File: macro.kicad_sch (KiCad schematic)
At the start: 27 parts, among them J1 USB_C_Receptacle_USB2.0, SW1 SW_Push, U1 ATmega32U4-A, Y1 16MHz

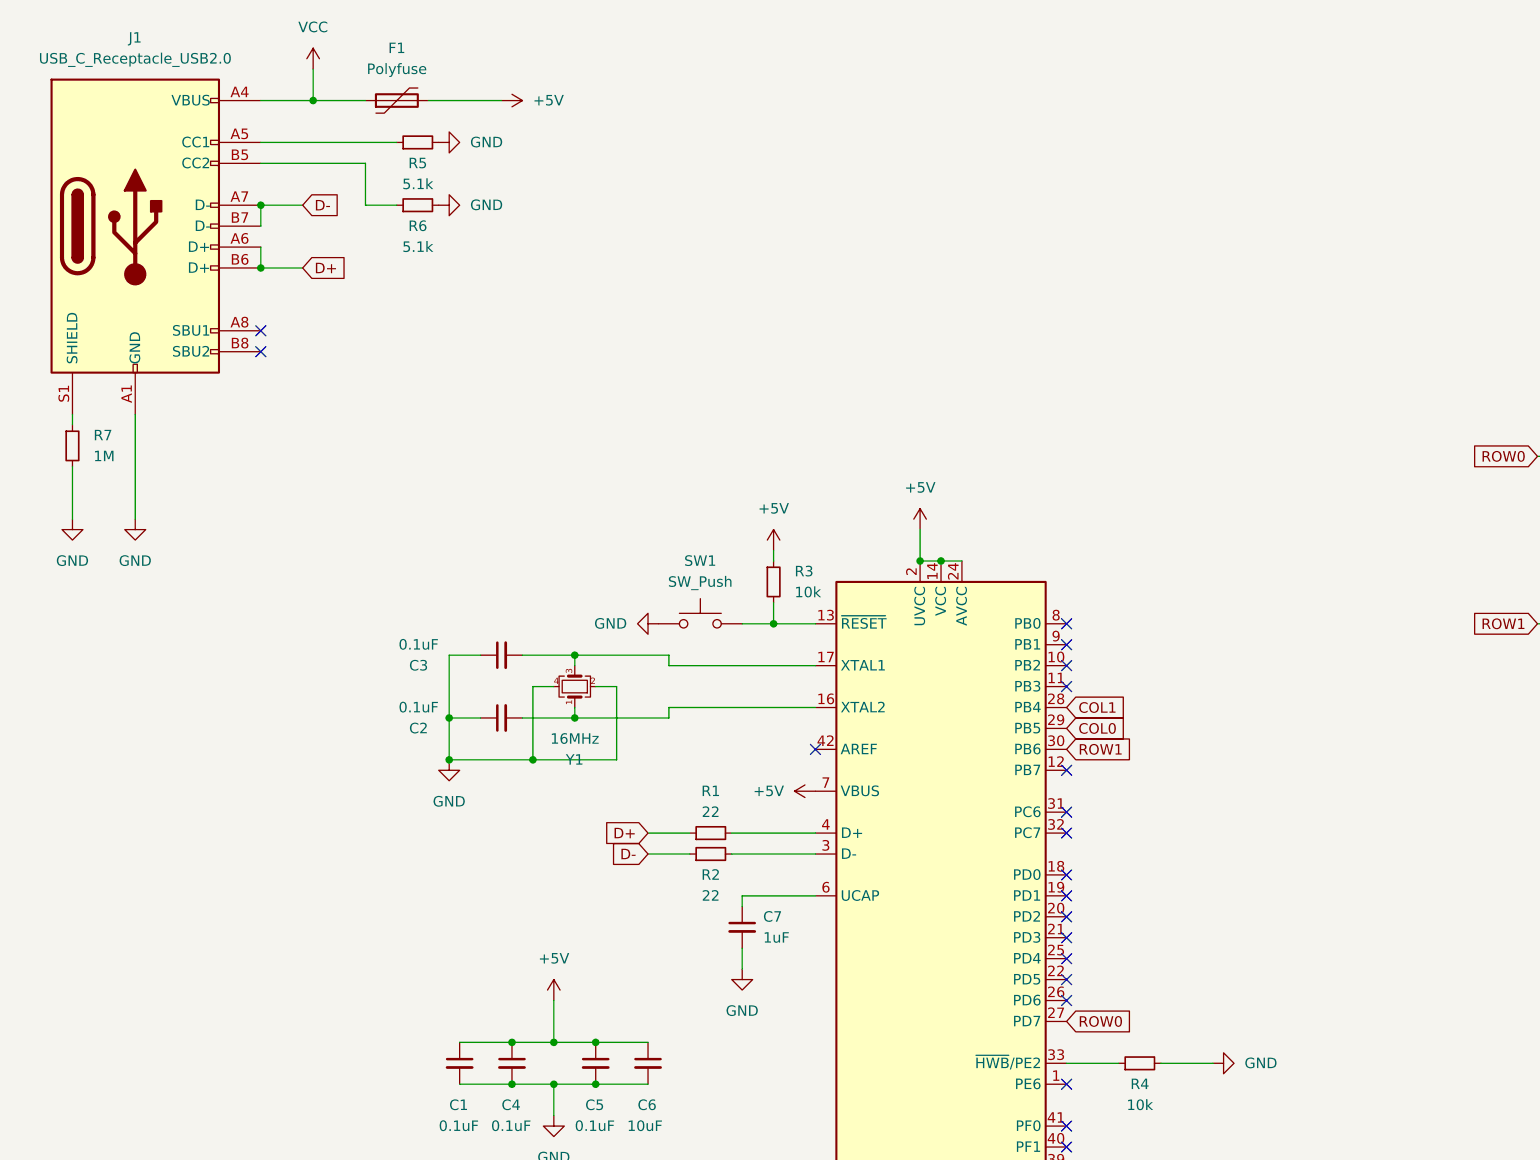
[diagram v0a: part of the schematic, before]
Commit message: Add ws2812
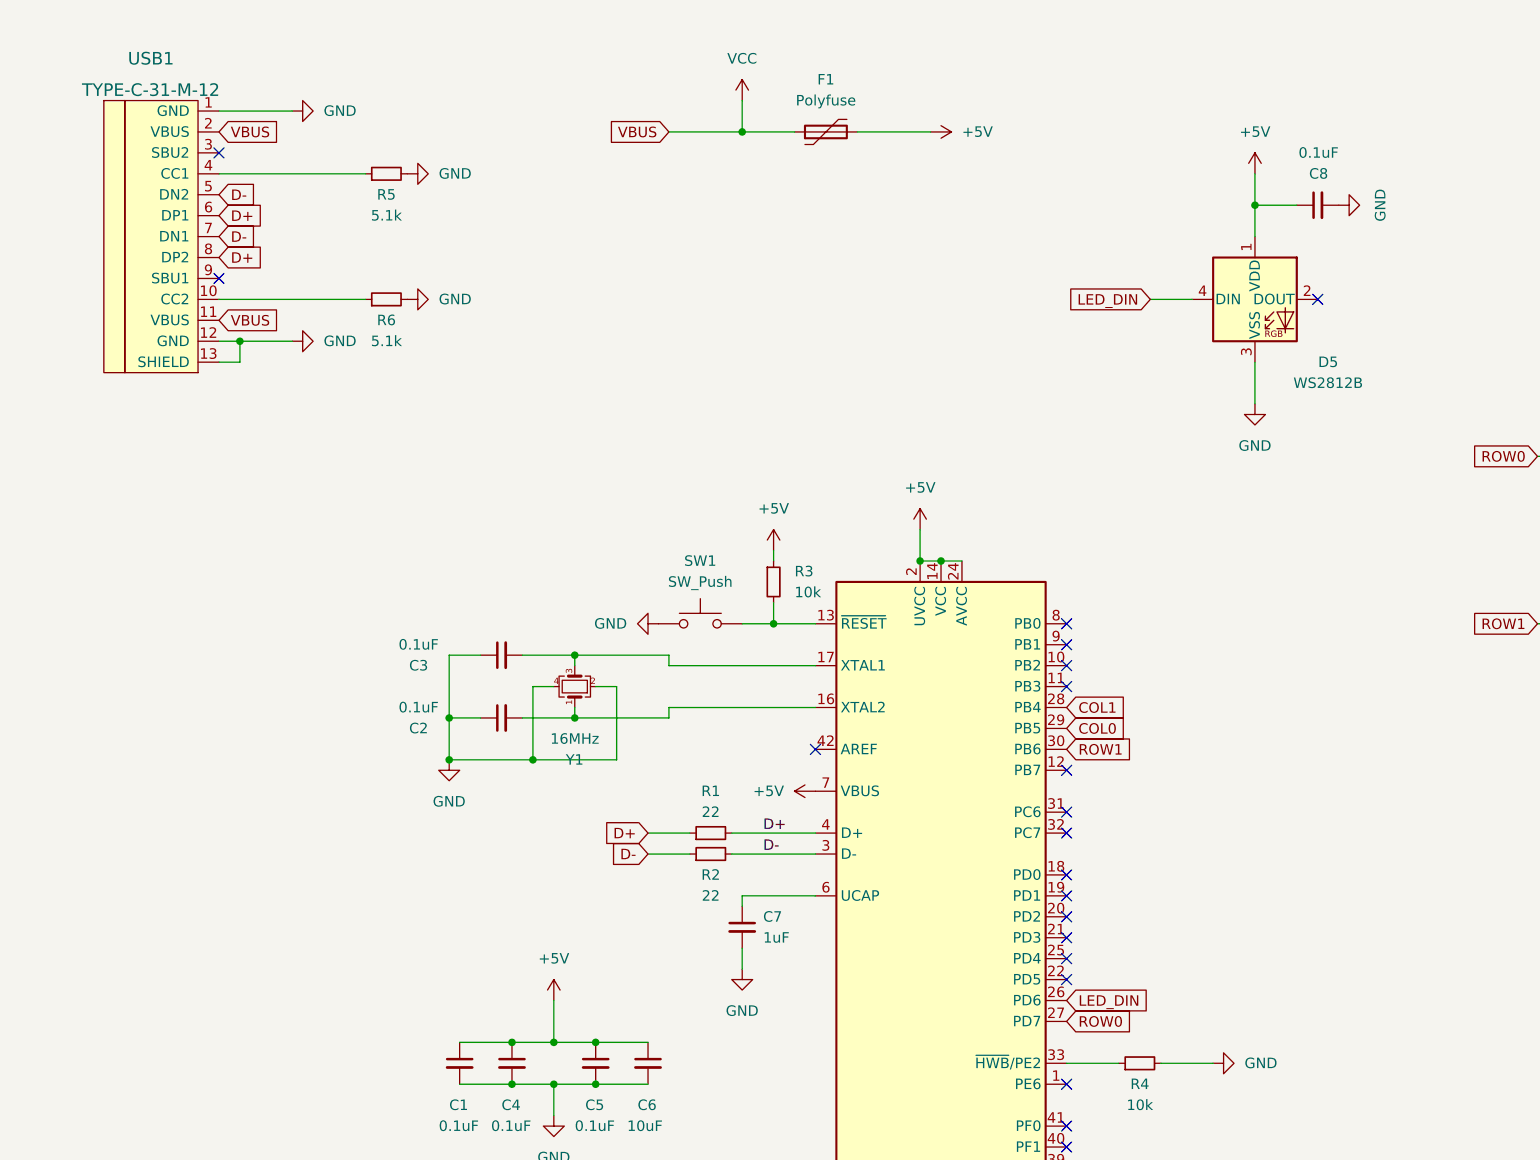
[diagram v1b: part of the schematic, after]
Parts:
- removed J1: USB_C_Receptacle_USB2.0, 105450-0101:MOLEX_105450-0101, symbol Connector:USB_C_Receptacle_USB2.0
- removed R7: 1M, Resistor_SMD:R_0805_2012Metric, symbol Device:R_Small
- added C8: 0.1uF, Capacitor_SMD:C_0805_2012Metric_Pad1.18x1.45mm_HandSolder, symbol Device:C_Small
- added D5: WS2812B, LED_SMD:LED_WS2812B_PLCC4_5.0x5.0mm_P3.2mm, symbol LED:WS2812B
- added USB1: TYPE-C-31-M-12, Type-C:HRO-TYPE-C-31-M-12-Assembly, symbol Type-C:HRO-TYPE-C-31-M-12
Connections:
- net +5V: now also C8.1, D5.1 (VDD)
- net D+: now also R1.2, U1.4 (D+), USB1.6 (DP1), USB1.8 (DP2)
- net D-: now also R2.2, U1.3 (D-), USB1.5 (DN2), USB1.7 (DN1)
- net GND: now also C8.2, D5.3 (VSS), USB1.1 (GND), USB1.12 (GND), USB1.13 (SHIELD)
- net VCC: now also USB1.11 (VBUS), USB1.2 (VBUS)
- net at R5.1: now also USB1.4 (CC1)
- net at R6.1: now also USB1.10 (CC2)
- net LED_DIN: now reaches U1.26 (PD6)
- net LED_DIN: now also D5.4 (DIN)
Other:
- moved on the sheet: F1, R5, R6

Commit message: New design
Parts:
- removed D5: WS2812B, LED_SMD:LED_WS2812B_PLCC4_5.0x5.0mm_P3.2mm, symbol LED:WS2812B
- removed U1: ATmega32U4-A, Package_QFP:TQFP-44_10x10mm_P0.8mm, symbol MCU_Microchip_ATmega:ATmega32U4-A
- added C10: 10nF, Capacitor_SMD:C_0402_1005Metric, symbol Device:C_Small
- added C11, C12, C13, C14, C15, C16, C9: 100nF, Capacitor_SMD:C_0402_1005Metric, symbol Device:C_Small
- added C17, C18: 30pF, Capacitor_SMD:C_0402_1005Metric, symbol Device:C_Small
- added D5: D_Small, Diode_SMD:D_SOD-323, symbol Device:D_Small
- added D6: D_Schottky_Small, Diode_SMD:D_SOD-323, symbol Device:D_Schottky_Small
- added H1, H2, H3, H4: MountingHole, MountingHole:MountingHole_2.2mm_M2, symbol Mechanical:MountingHole
- added J1, J2, J3: Conn_01x01_Male, TestPoint:TestPoint_Pad_2.0x2.0mm, symbol Connector:Conn_01x01_Male
- added R7: 10k, Resistor_SMD:R_0402_1005Metric, symbol Device:R_Small
- added R8: 1K, Resistor_SMD:R_0402_1005Metric, symbol Device:R_Small
- added SW2: RotaryEncoder_Switch, Rotary_Encoder:RotaryEncoder_Alps_EC11E-Switch_Vertical_H20mm_CircularMountingHoles, symbol Device:RotaryEncoder_Switch
- added SW3: SW_Push, Button_Switch_SMD:SW_Push_1P1T_NO_CK_KMR2, symbol Switch:SW_Push
- added U1: RP2040, Package_DFN_QFN:QFN-56-1EP_7x7mm_P0.4mm_EP3.2x3.2mm, symbol rp2040:RP2040
- added U2: AP2112K-3.3, Package_TO_SOT_SMD:SOT-23-5, symbol Regulator_Linear:AP2112K-3.3
- added U3: W25Q128JVPIQ, Package_SON:WSON-8-1EP_6x5mm_P1.27mm_EP3.4x4.3mm, symbol Memory_Flash:W25Q32JVZP
- C1: value 0.1uF -> 10uF; footprint Capacitor_SMD:C_0805_2012Metric_Pad1.18x1.45mm_HandSolder -> Capacitor_SMD:C_0402_1005Metric
- C2, C4, C5: value 0.1uF -> 100nF; footprint Capacitor_SMD:C_0805_2012Metric_Pad1.18x1.45mm_HandSolder -> Capacitor_SMD:C_0402_1005Metric
- C3: value 0.1uF -> 1uF; footprint Capacitor_SMD:C_0805_2012Metric_Pad1.18x1.45mm_HandSolder -> Capacitor_SMD:C_0402_1005Metric
- C6: value 10uF -> 1uF; footprint Capacitor_SMD:C_0805_2012Metric_Pad1.18x1.45mm_HandSolder -> Capacitor_SMD:C_0402_1005Metric
- C7: value 1uF -> 10uF; footprint Capacitor_SMD:C_0805_2012Metric_Pad1.18x1.45mm_HandSolder -> Capacitor_SMD:C_0402_1005Metric
- C8: value 0.1uF -> 10nF; footprint Capacitor_SMD:C_0805_2012Metric_Pad1.18x1.45mm_HandSolder -> Capacitor_SMD:C_0402_1005Metric
- D1, D2, D3, D4: footprint Diode_SMD:D_SOD-123 -> Diode_SMD:D_SOD-323
- F1: footprint Fuse:Fuse_1206_3216Metric -> Fuse:Fuse_0402_1005Metric
- R1, R2: value 22 -> 27.4; footprint Resistor_SMD:R_0805_2012Metric -> Resistor_SMD:R_0402_1005Metric
- R3: value 10k -> 1K; footprint Resistor_SMD:R_0805_2012Metric -> Resistor_SMD:R_0402_1005Metric
- R4, R5, R6: footprint Resistor_SMD:R_0805_2012Metric -> Resistor_SMD:R_0402_1005Metric
- SW1: footprint random-keyboard-parts:SKQG-1155865 -> Button_Switch_SMD:SW_Push_1P1T_NO_CK_KMR2
- Y1: value 16MHz -> 12MHz
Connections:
- net COL0: now also SW2.S1, U1.5 (GPIO3)
- net COL1: now also U1.6 (GPIO4)
- net D+: no longer R1.1, R1.2
- net D-: no longer R2.1, R2.2
- net GND: now also C2.2, C3.2, SW1.2, C10.1, C11.2, C12.2, C13.2, C14.2, C15.2, C16.2, C17.1, C18.1, C9.2, J1.1 (Pin_1), SW2.C, SW3.2, U1.19 (TESTEN), U1.57 (GND), U2.2 (GND), U3.4 (GND), U3.9 (EP); no longer C2.1, C3.1, R4.2, SW1.1, USB1.13 (SHIELD)
- net ROW0: now also U1.2 (GPIO0)
- net ROW1: now also U1.3 (GPIO1)
- net at Y1.1: now also C18.2, R8.1; no longer C2.2
- net XIN: now reaches Y1.3
- net XIN: now also C17.2, U1.20 (XIN); no longer C3.2
- net QSPI_SS: now reaches R3.2
- net QSPI_SS: now also R7.2, U1.56 (QSPI_SS), U3.1 (~{CS}); no longer SW1.2
- net +3.3V: now reaches C7.1
- net +3.3V: now also C2.1, C3.1, C4.1, C5.1, R4.1, C11.1, C13.1, C15.1, C16.1, C9.1, R7.1, U1.1 (IOVDD), U1.10 (IOVDD), U1.22 (IOVDD), U1.33 (IOVDD), U1.42 (IOVDD), U1.43 (ADC_AVDD), U1.44 (VREG_IN), U1.48 (USB_VDD), U1.49 (IOVDD), U2.5 (VOUT), U3.8 (VCC)
- removed net +5V: C1.1, C4.1, C5.1, C6.1, C8.1, F1.2, R3.1
- net VCC renamed VBUS
- new net: C1.1, D6.1 (K), U2.1 (VIN), U2.3 (EN)
- new net: D6.2 (A), F1.2
- new net: R1.2, U1.47 (USB_DP)
- new net: R2.2, U1.46 (USB_DM)
- new net: D5.2 (A), SW2.S2
- new net +1V1: C12.1, C14.1, C6.1, U1.23 (DVDD), U1.45 (VREG_VOUT), U1.50 (DVDD)
- new net BOOTSEL: R3.1, SW3.1
- new net QSPI_CLK: U1.52 (QSPI_SCLK), U3.6 (CLK)
- new net QSPI_SD0: U1.53 (QSPI_SD0), U3.5 (DI(IO0))
- new net QSPI_SD1: U1.55 (QSPI_SD1), U3.2 (DO(IO1))
- new net QSPI_SD2: U1.54 (QSPI_SD2), U3.3 (IO2)
- new net QSPI_SD3: U1.51 (QSPI_SD3), U3.7 (IO3)
- new net RESET: R4.2, SW1.1, U1.26 (RUN)
- new net ROT0: C8.1, SW2.A, U1.7 (GPIO5)
- new net ROT1: C10.2, SW2.B, U1.8 (GPIO6)
- new net ROW2: D5.1 (K), U1.4 (GPIO2)
- new net SWCLK: J3.1 (Pin_1), U1.24 (SWCLK)
- new net SWD: J2.1 (Pin_1), U1.25 (SWD)
- new net USB_D+: R1.1
- new net USB_D-: R2.1
- new net XOUT: R8.2, U1.21 (XOUT)
- no-connect marks 24 -> 26
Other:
- note added: "80 OHM ESR 20 pF Load capacitance 5 pF Parasitic capacitance (20 - 5)*2 = 30 pF"
- note added: "These should be close to the rp2040"
- moved on the sheet: D1, D2, D3, D4, MX1, MX2, MX3, MX4, R5, R6, USB1
